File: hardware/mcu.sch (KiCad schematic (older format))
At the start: 52 parts, among them J1 ADc, J2 Conn_01x04_Male, J3 Micro_SD_Card, J4 BOOT0, J5 Conn_01x03_Male, J6 display, SW1 SW_right, SW2 SW_right, SW3 SW_middle2, SW4 SW_top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

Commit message: trwa układanie, dodane złacze golpin
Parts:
- renumbered SW1 to SW_rst1
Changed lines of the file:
@@
 	1800 4250 1950 4250
 $Comp
-L Switch:SW_Push SW1
+L Switch:SW_Push SW_rst1
 U 1 1 5CF329C5
 P 4550 2800
-F 0 "SW1" H 4550 3085 50  0000 C CNN
+F 0 "SW_rst1" H 4550 3085 50  0000 C CNN
 F 1 "SW_right" H 4550 2994 50  0000 C CNN
 F 2 "Button_Switch_SMD:SW_Push_1P1T_NO_CK_KSC6xxJ" H 4550 3000 50  0001 C CNN

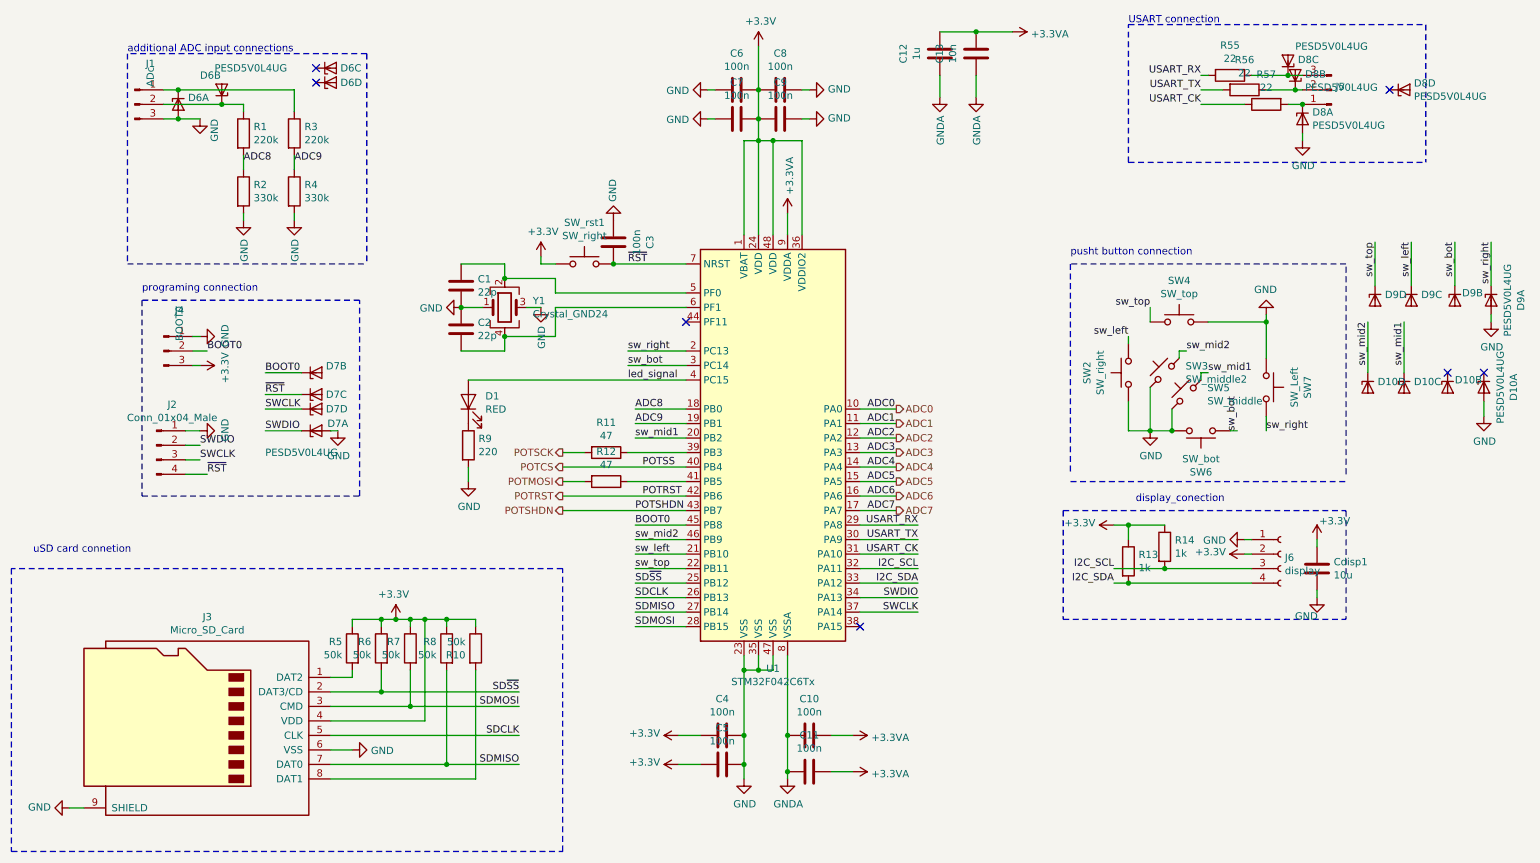
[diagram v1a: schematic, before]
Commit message: layout gotów, do wyeliminowania błedy DRC
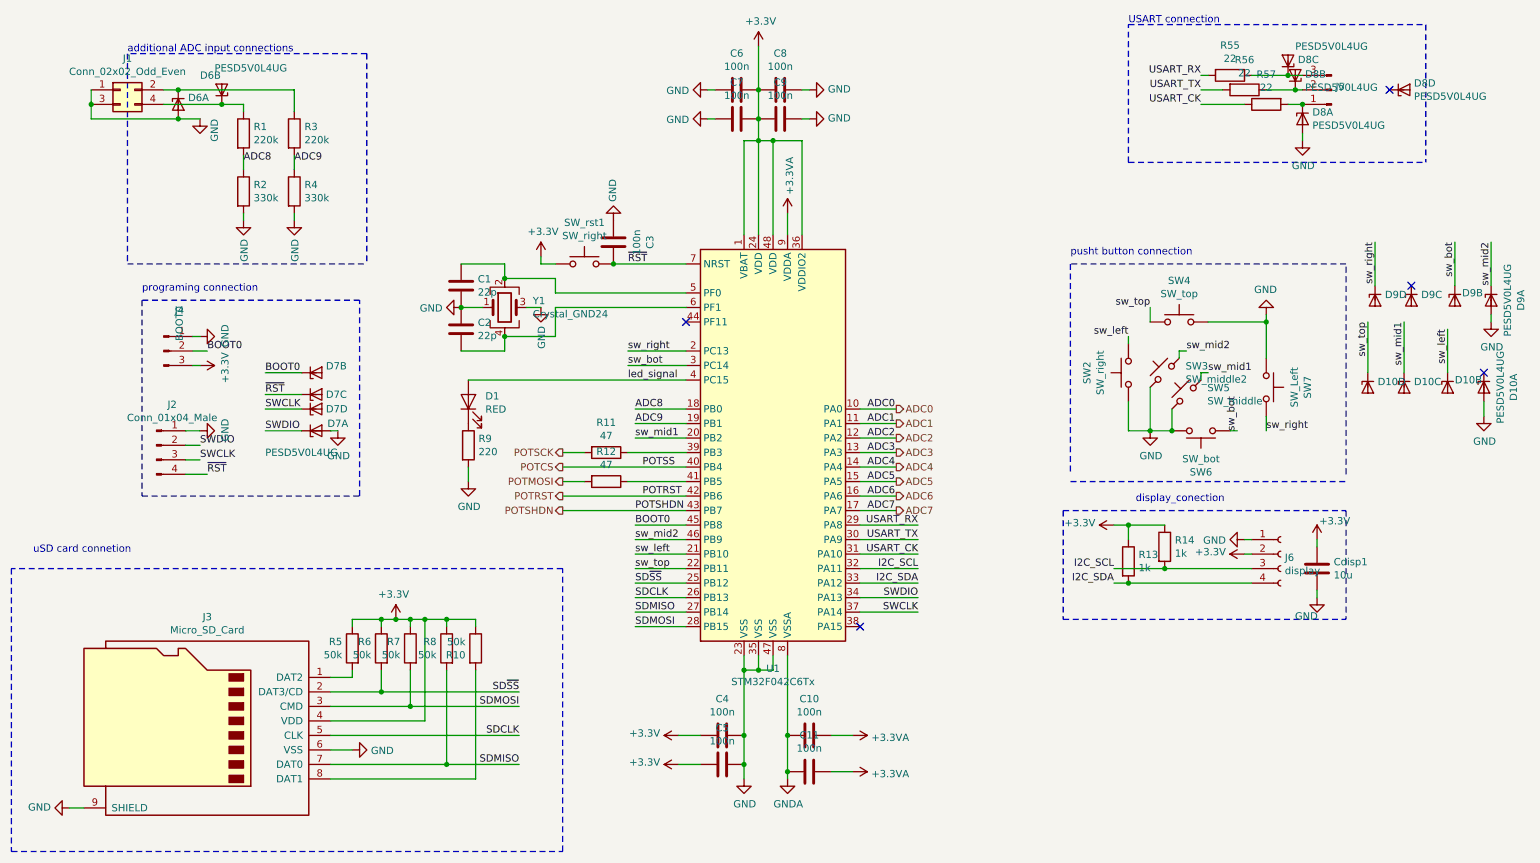
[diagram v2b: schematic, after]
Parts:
- removed C12: 1u, Capacitor_SMD:C_0603_1608Metric_Pad1.05x0.95mm_HandSolder, symbol Device:C
- removed C13: 10n, Capacitor_SMD:C_0603_1608Metric_Pad1.05x0.95mm_HandSolder, symbol Device:C
- removed unit 3 of D6
- removed unit 4 of D6
- removed J1: ADc, Connector_PinHeader_2.54mm:PinHeader_1x03_P2.54mm_Vertical, symbol Connector:Conn_01x03_Male
- added J1: Conn_02x02_Odd_Even, Connector_PinHeader_2.54mm:PinHeader_2x02_P2.54mm_Vertical, symbol Connector_Generic:Conn_02x02_Odd_Even
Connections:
- net GND: now also J1.1 (Pin_1), J1.3 (Pin_3)
- net sw_left: now also D10.3 (K2); no longer D9.4 (K3)
- net sw_mid2: now also D9.1 (K1); no longer D10.5 (K4)
- net sw_right: now also D9.5 (K4); no longer D9.1 (K1)
- net sw_top: now also D10.5 (K4); no longer D9.5 (K4)
- net at D6.1 (K1), R3.1: now also J1.2 (Pin_2)
- net at D6.3 (K2), R1.1: now also J1.4 (Pin_4)
- no-connect marks 7 -> 5
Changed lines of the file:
@@
 	0    1    1    0
-$EndComp
-Wire Wire Line
-	7000 1650 7000 1500
-Wire Wire Line
-	7250 1650 7250 1500
-Connection ~ 7250 1200
-$Comp
-L Device:C C13
-U 1 1 5CEA12AD
-P 7250 1350
-F 0 "C13" V 6998 1350 50  0000 C CNN
-F 1 "10n" V 7089 1350 50  0000 C CNN
-F 2 "Capacitor_SMD:C_0603_1608Metric_Pad1.05x0.95mm_HandSolder" H 7288 1200 50  0001 C CNN
-F 3 "~" H 7250 1350 50  0001 C CNN
-	1    7250 1350
-	1    0    0    -1
-$EndComp
-Wire Wire Line
-	7000 1200 7250 1200
-$Comp
-L Device:C C12
-U 1 1 5CE95807
-P 7000 1350
-F 0 "C12" V 6748 1350 50  0000 C CNN
-F 1 "1u" V 6839 1350 50  0000 C CNN
-F 2 "Capacitor_SMD:C_0603_1608Metric_Pad1.05x0.95mm_HandSolder" H 7038 1200 50  0001 C CNN
-F 3 "~" H 7000 1350 50  0001 C CNN
-	1    7000 1350
-	1    0    0    -1
 $EndComp
 $Comp
@@
 	0    -1   -1   0
 $EndComp
-$Comp
-L power:+3.3VA #PWR029
-U 1 1 5CEA97D8
-P 7500 1200
-F 0 "#PWR029" H 7500 1050 50  0001 C CNN
-F 1 "+3.3VA" V 7515 1328 50  0000 L CNN
-F 2 "" H 7500 1200 50  0001 C CNN
-F 3 "" H 7500 1200 50  0001 C CNN
-	1    7500 1200
-	0    1    1    0
-$EndComp
-Wire Wire Line
-	7250 1200 7500 1200
 $Comp
 L power:+3.3VA #PWR021
@@
 NoConn ~ 5250 3200
 $Comp
-L power:GNDA #PWR028
-U 1 1 5CEA12B3
-P 7250 1650
-F 0 "#PWR028" H 7250 1400 50  0001 C CNN
-F 1 "GNDA" V 7255 1523 50  0000 R CNN
-F 2 "" H 7250 1650 50  0001 C CNN
-F 3 "" H 7250 1650 50  0001 C CNN
-	1    7250 1650
-	1    0    0    -1
-$EndComp
-$Comp
-L power:GNDA #PWR027
-U 1 1 5CE9FB9E
-P 7000 1650
-F 0 "#PWR027" H 7000 1400 50  0001 C CNN
-F 1 "GNDA" V 7005 1523 50  0000 R CNN
-F 2 "" H 7000 1650 50  0001 C CNN
-F 3 "" H 7000 1650 50  0001 C CNN
-	1    7000 1650
-	1    0    0    -1
-$EndComp
-$Comp
 L power:+3.3V #PWR020
 U 1 1 5CE9321B
@@
 Wire Wire Line
 	4850 3500 5250 3500
-$Comp
-L Connector:Conn_01x03_Male J1
-U 1 1 5CE37969
-P 1450 1700
-F 0 "J1" H 1558 1981 50  0000 C CNN
-F 1 "ADc" V 1558 1890 50  0000 C CNN
-F 2 "Connector_PinHeader_2.54mm:PinHeader_1x03_P2.54mm_Vertical" H 1450 1700 50  0001 C CNN
-F 3 "~" H 1450 1700 50  0001 C CNN
-	1    1450 1700
-	1    0    0    -1
-$EndComp
 Wire Notes Line
 	1400 2800 3050 2800
@@
 Wire Wire Line
 	1900 1800 1750 1800
-Wire Wire Line
-	1750 1800 1650 1800
 Connection ~ 1750 1800
 Wire Wire Line
@@
 $EndComp
 $Comp
-L Power_Protection:PESD5V0L4UG D6
-U 3 1 5D505F16
-P 2800 1450
-F 0 "D6" H 2868 1450 50  0000 L CNN
-F 1 "PESD5V0L4UG" H 2868 1405 50  0001 L CNN
-F 2 "Package_TO_SOT_SMD:SOT-353_SC-70-5" H 2800 1450 50  0001 C CNN
-F 3 "https://assets.nexperia.com/documents/data-sheet/PESDXL4UF_G_W.pdf" H 2800 1450 50  0001 C CNN
-	3    2800 1450
-	1    0    0    -1
-$EndComp
-$Comp
-L Power_Protection:PESD5V0L4UG D6
-U 4 1 5D506693
-P 2800 1550
-F 0 "D6" H 2868 1550 50  0000 L CNN
-F 1 "PESD5V0L4UG" H 2868 1505 50  0001 L CNN
-F 2 "Package_TO_SOT_SMD:SOT-353_SC-70-5" H 2800 1550 50  0001 C CNN
-F 3 "https://assets.nexperia.com/documents/data-sheet/PESDXL4UF_G_W.pdf" H 2800 1550 50  0001 C CNN
-	4    2800 1550
-	1    0    0    -1
-$EndComp
-NoConn ~ 2700 1450
-NoConn ~ 2700 1550
-$Comp
 L Power_Protection:PESD5V0L4UG D7
 U 1 1 5D55BD94
@@
 	1    0    0    -1
 $EndComp
-Text Label 10800 2650 3    50   ~ 0
+Text Label 10000 2650 3    50   ~ 0
 sw_right
 Text Label 10550 2650 3    50   ~ 0
@@
 Text Label 10200 3200 3    50   ~ 0
 sw_mid1
+Text Label 10800 2650 3    50   ~ 0
+sw_mid2
 Text Label 9950 3200 3    50   ~ 0
-sw_mid2
-Text Label 10000 2650 3    50   ~ 0
 sw_top
-Text Label 10250 2650 3    50   ~ 0
+Text Label 10500 3250 3    50   ~ 0
 sw_left
 $Comp
@@
 	10000 2950 10000 2650
 Wire Wire Line
-	10250 2650 10250 2950
+	10500 3250 10500 3550
 Wire Wire Line
 	10550 2950 10550 2650
@@
 Wire Wire Line
 	10750 3850 10750 3750
-NoConn ~ 10500 3550
 NoConn ~ 10750 3550
+$Comp
+L Connector_Generic:Conn_02x02_Odd_Even J1
+U 1 1 5DB034FE
+P 1350 1600
+F 0 "J1" H 1400 1817 50  0000 C CNN
+F 1 "Conn_02x02_Odd_Even" H 1400 1726 50  0000 C CNN
+F 2 "Connector_PinHeader_2.54mm:PinHeader_2x02_P2.54mm_Vertical" H 1350 1600 50  0001 C CNN
+F 3 "~" H 1350 1600 50  0001 C CNN
+	1    1350 1600
+	1    0    0    -1
+$EndComp
+Wire Wire Line
+	1150 1600 1150 1700
+Wire Wire Line
+	1150 1700 1150 1800
+Wire Wire Line
+	1150 1800 1750 1800
+Connection ~ 1150 1700
+NoConn ~ 10250 2950
 $EndSCHEMATC

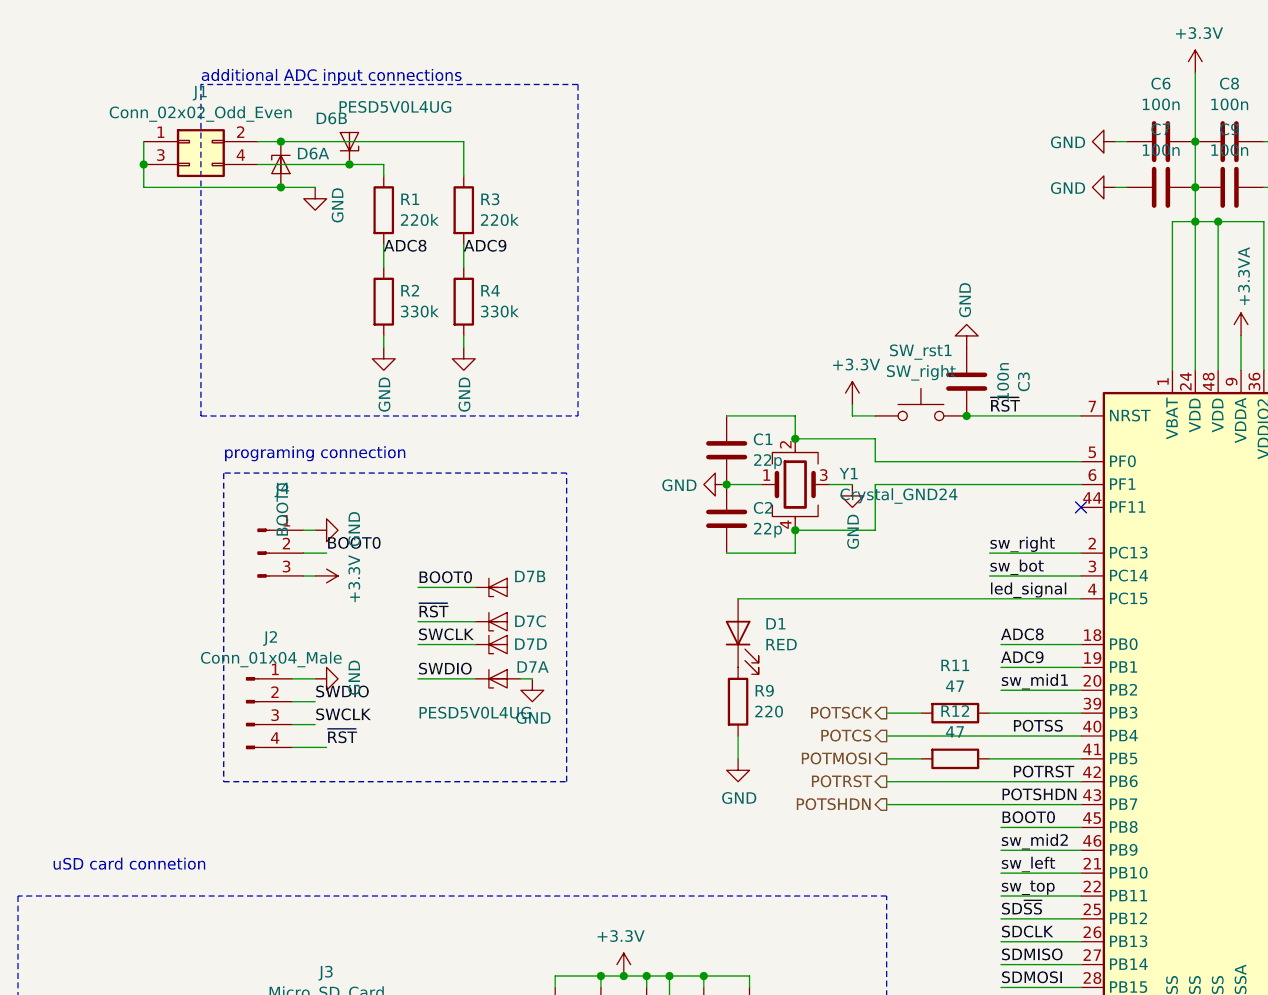
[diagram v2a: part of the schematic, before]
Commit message: dodano poprawki błędów znalezionych podczas montażu
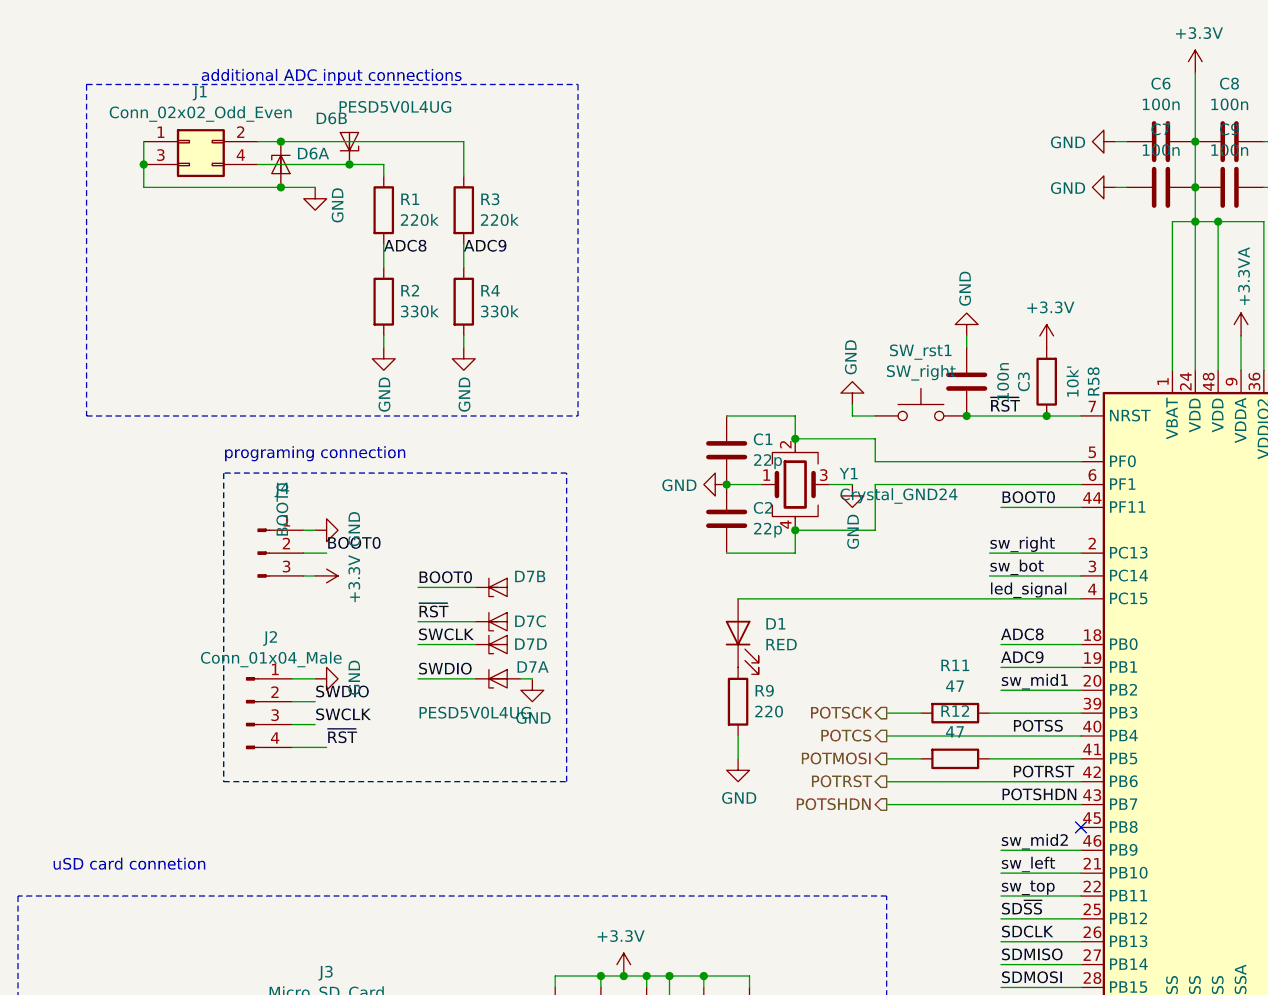
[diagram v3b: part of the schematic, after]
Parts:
- added R58: 10k', Resistor_SMD:R_0603_1608Metric_Pad1.05x0.95mm_HandSolder, symbol Device:R
- Y1: footprint Crystal:Crystal_SMD_3225-4Pin_3.2x2.5mm -> symbols:Crystal_SMD_3225-4Pin_3.2x2.5mm
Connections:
- net +3V3: now also R58.2; no longer SW_rst1.1
- net BOOT0: now also U1.44 (PF11); no longer U1.45 (PB8)
- net GND: now also SW_rst1.1
- net ~RST: now also R58.1
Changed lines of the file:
@@
 $EndComp
 Wire Wire Line
-	5250 2800 4750 2800
+	5250 2800 5100 2800
 $Comp
 L power:GND #PWR014
 U 1 1 5CE5FAB4
-P 4750 2500
-F 0 "#PWR014" H 4750 2250 50  0001 C CNN
-F 1 "GND" V 4755 2372 50  0000 R CNN
-F 2 "" H 4750 2500 50  0001 C CNN
-F 3 "" H 4750 2500 50  0001 C CNN
-	1    4750 2500
+P 4250 2750
+F 0 "#PWR014" H 4250 2500 50  0001 C CNN
+F 1 "GND" V 4255 2622 50  0000 R CNN
+F 2 "" H 4250 2750 50  0001 C CNN
+F 3 "" H 4250 2750 50  0001 C CNN
+	1    4250 2750
 	-1   0    0    1
 $EndComp
@@
 Wire Wire Line
 	6450 5200 6850 5200
-Text Label 4900 4600 0    50   ~ 0
+Text Label 4900 3200 0    50   ~ 0
 BOOT0
 $Comp
@@
 	1900 3500 1850 3500
 Wire Wire Line
-	4900 4600 5250 4600
+	4900 3200 5250 3200
 Text Label 1950 3400 0    50   ~ 0
 BOOT0
@@
 	1    0    0    -1
 $EndComp
-$Comp
-L power:+3.3V #PWR012
-U 1 1 5CF39DCC
-P 4250 2750
-F 0 "#PWR012" H 4250 2600 50  0001 C CNN
-F 1 "+3.3V" H 4265 2923 50  0000 C CNN
-F 2 "" H 4250 2750 50  0001 C CNN
-F 3 "" H 4250 2750 50  0001 C CNN
-	1    4250 2750
-	1    0    0    -1
-$EndComp
 Wire Wire Line
 	4350 2800 4250 2800
@@
 Wire Wire Line
 	6450 4900 6850 4900
-NoConn ~ 5250 3200
 $Comp
 L power:+3.3V #PWR020
@@
 Wire Wire Line
 	4850 3500 5250 3500
-Wire Notes Line
-	1400 2800 3050 2800
 $Comp
 L Device:Crystal_GND24 Y1
@@
 F 0 "Y1" H 4194 3146 50  0000 L CNN
 F 1 "Crystal_GND24" H 4194 3055 50  0000 L CNN
-F 2 "Crystal:Crystal_SMD_3225-4Pin_3.2x2.5mm" H 4000 3100 50  0001 C CNN
+F 2 "symbols:Crystal_SMD_3225-4Pin_3.2x2.5mm" H 4000 3100 50  0001 C CNN
 F 3 "https://www.tme.eu/pl/details/abm8-16.000mhz-b2/rezonatory-kwarcowe-smd/abracon/abm8-16-000mhz-b2-t/" H 4000 3100 50  0001 C CNN
 	1    4000 3100
@@
 additional ADC input connections\n
 Wire Notes Line
-	3050 1350 1400 1350
-Wire Notes Line
-	1400 1350 1400 2800
+	900  1350 900  2800
 Wire Notes Line
 	3050 1350 3050 2800
@@
 Connection ~ 1150 1700
 NoConn ~ 10250 2950
+NoConn ~ 5250 4600
+$Comp
+L Device:R R58
+U 1 1 5D086583
+P 5100 2650
+F 0 "R58" V 4893 2650 50  0000 C CNN
+F 1 "10k'" V 4984 2650 50  0000 C CNN
+F 2 "Resistor_SMD:R_0603_1608Metric_Pad1.05x0.95mm_HandSolder" V 5030 2650 50  0001 C CNN
+F 3 "~" H 5100 2650 50  0001 C CNN
+	1    5100 2650
+	-1   0    0    1
+$EndComp
+Connection ~ 5100 2800
+Wire Wire Line
+	5100 2800 4750 2800
+$Comp
+L power:+3.3V #PWR0147
+U 1 1 5D086A3D
+P 5100 2500
+F 0 "#PWR0147" H 5100 2350 50  0001 C CNN
+F 1 "+3.3V" H 5115 2673 50  0000 C CNN
+F 2 "" H 5100 2500 50  0001 C CNN
+F 3 "" H 5100 2500 50  0001 C CNN
+	1    5100 2500
+	1    0    0    -1
+$EndComp
+Wire Notes Line
+	900  1350 3050 1350
+Wire Notes Line
+	900  2800 3050 2800
+$Comp
+L power:GND #PWR?
+U 1 1 5D0B54E3
+P 4750 2450
+F 0 "#PWR?" H 4750 2200 50  0001 C CNN
+F 1 "GND" V 4755 2322 50  0000 R CNN
+F 2 "" H 4750 2450 50  0001 C CNN
+F 3 "" H 4750 2450 50  0001 C CNN
+	1    4750 2450
+	-1   0    0    1
+$EndComp
+Wire Wire Line
+	4750 2500 4750 2450
 $EndSCHEMATC
